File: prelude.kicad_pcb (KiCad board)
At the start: 2 copper layers, 0 parts

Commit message: Several changes
Ran CvPcb
Added MicroSD card connector (Molex)
Started PCB routing with MCU pin row pins 1-16 facing 50-pin LCD connector
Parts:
- added C1: 8p, Capacitors_SMD:C_0805, F.Cu at (194.1, 133.0)
- added C10: 100n, Capacitors_SMD:C_0805, F.Cu at (191.9, 127.6)
- added C11: 22u, Capacitors_SMD:C_0805, F.Cu at (203.4, 119.1)
- added C12: 100n, Capacitors_SMD:C_0805, F.Cu at (208.8, 112.8)
- added C13: 100n, Capacitors_SMD:C_0805, F.Cu at (196.1, 127.5)
- added C14: 1uF, Capacitors_SMD:C_0805, F.Cu at (190.1, 133.3)
- added C15: 1uF, Capacitors_SMD:C_0805, F.Cu at (200.2, 124.4)
- added C2: 8p, Capacitors_SMD:C_0805, F.Cu at (187.8, 127.9)
- added C3: 100n, Capacitors_SMD:C_0805, F.Cu at (207.5, 107.5)
- added C4: 10uF, Capacitors_SMD:C_0805, F.Cu at (200.7, 113.8)
- added C5: 100n, Capacitors_SMD:C_0805, F.Cu at (181.9, 133.4)
- added C6: 1u, Capacitors_SMD:C_0805, F.Cu at (195.2, 122.2)
- added C7: 10u, Capacitors_SMD:C_0805, F.Cu at (204.7, 113.8)
- added C8: 100n, Capacitors_SMD:C_0805, F.Cu at (186.1, 133.4)
- added C9: 100n, Capacitors_SMD:C_0805, F.Cu at (199.3, 119.1)
- added D1: LED, LEDs:LED_0805, F.Cu at (208.9, 118.1)
- added D2: MBR0530, Diodes_SMD:D_SOD-123, F.Cu at (186.0, 122.2)
- added F1: Polyfuse, volium:MF-PSMF050X, F.Cu at (202.0, 108.1)
- added J1: CONN_01X50, volium:62684-502100ALF, F.Cu at (121.7, 137.0)
- added J2: USB_C, volium:DX07S024XJ1, F.Cu at (114.8, 98.3)
- added J3: CONN_01X04, Pin_Headers:Pin_Header_Angled_1x04_Pitch2.54mm, F.Cu at (181.1, 108.3)
- added L1: 2.2uH, Inductors:Inductor_Taiyo-Yuden_NR-24xx, F.Cu at (194.3, 115.9)
- added L2: 22uH, Inductors:Inductor_Taiyo-Yuden_NR-30xx, F.Cu at (173.8, 133.0)
- added R1: 5K1, Resistors_SMD:R_0805, F.Cu at (177.8, 132.2)
- added R2: 5K1, Resistors_SMD:R_0805, F.Cu at (184.1, 128.1)
- added R3: 330, Resistors_SMD:R_0805, F.Cu at (191.4, 122.3)
- added R4: 2.55, Resistors_SMD:R_0805, F.Cu at (168.9, 133.8)
- added R5: 1.5K, Resistors_SMD:R_0805, F.Cu at (109.3, 108.6)
- added SW1: SW_Push, Buttons_Switches_SMD:SW_SPST_PTS645, F.Cu at (177.0, 124.3)
- added U1: LM3671MF-3.3, TO_SOT_Packages_SMD:TSOT-23-5, F.Cu at (153.5, 137.0)
- added U2: STM32F103RETx, Housings_QFP:LQFP-64_10x10mm_Pitch0.5mm, F.Cu at (116.5, 114.9)
- added U3: AP5724, TO_SOT_Packages_SMD:SOT-23-6, F.Cu at (164.0, 135.1)
- added XS1: Molex_microSD_1051620001, volium:Molex_1051620001, F.Cu at (86.4, 112.4)
- added Y1: 16MHz, Crystals:Crystal_SMD_5032-2pin_5.0x3.2mm, F.Cu at (195.3, 108.8)
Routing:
- net /LCD_DB15: track 0.00 -> 39.8 mm, vias 0 -> 2
- net /LCD_DB14: track 0.00 -> 39.4 mm, vias 0 -> 2
- net /LCD_DB13: track 0.00 -> 39.0 mm, vias 0 -> 2
- net /LCD_DB12: track 0.00 -> 38.5 mm, vias 0 -> 2
- net /SDIO_D1: track 0.00 -> 37.2 mm, vias 0 -> 2
- net /SDIO_D0: track 0.00 -> 37.1 mm, vias 0 -> 2
- net /LCD_DB11: track 0.00 -> 35.6 mm, vias 0 -> 2
- net /LCD_RD: track 0.00 -> 35.4 mm
- net /LCD_WR: track 0.00 -> 34.3 mm
- net /LCD_DB3: track 0.00 -> 31.3 mm, vias 0 -> 2
- net /LCD_DB4: track 0.00 -> 30.4 mm, vias 0 -> 2
- net /SDIO_D2: track 0.00 -> 30.1 mm, vias 0 -> 2
- net /LCD_DB5: track 0.00 -> 29.1 mm, vias 0 -> 2
- net /SDIO_D3: track 0.00 -> 28.9 mm, vias 0 -> 2
- net /SDIO_CLK: track 0.00 -> 28.5 mm
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
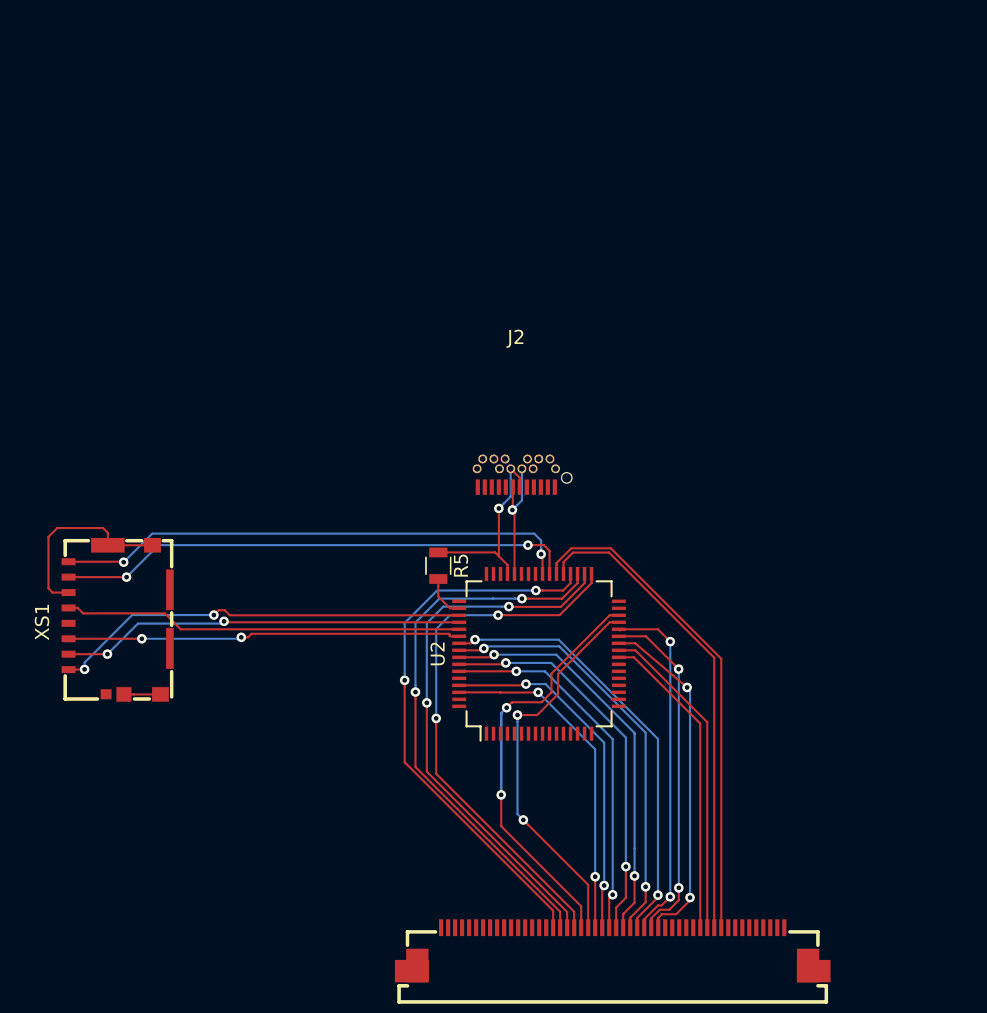
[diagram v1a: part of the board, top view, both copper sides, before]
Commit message: Moved to STM32F411RE
Had to move to different MCU (STM32F411RE) because I2C bus was fixed to pins on B bus, which was used for LCD data bus, and SDIO was also fixed to C bus.
Remapped LCD data bus to C bus since it allows having all other functionality (SDIO, I2C, USB) correctly mapped.
Redid CvPcb and net generation.
Started PCB routing with MCU pins 49-64 facing LCD connector.
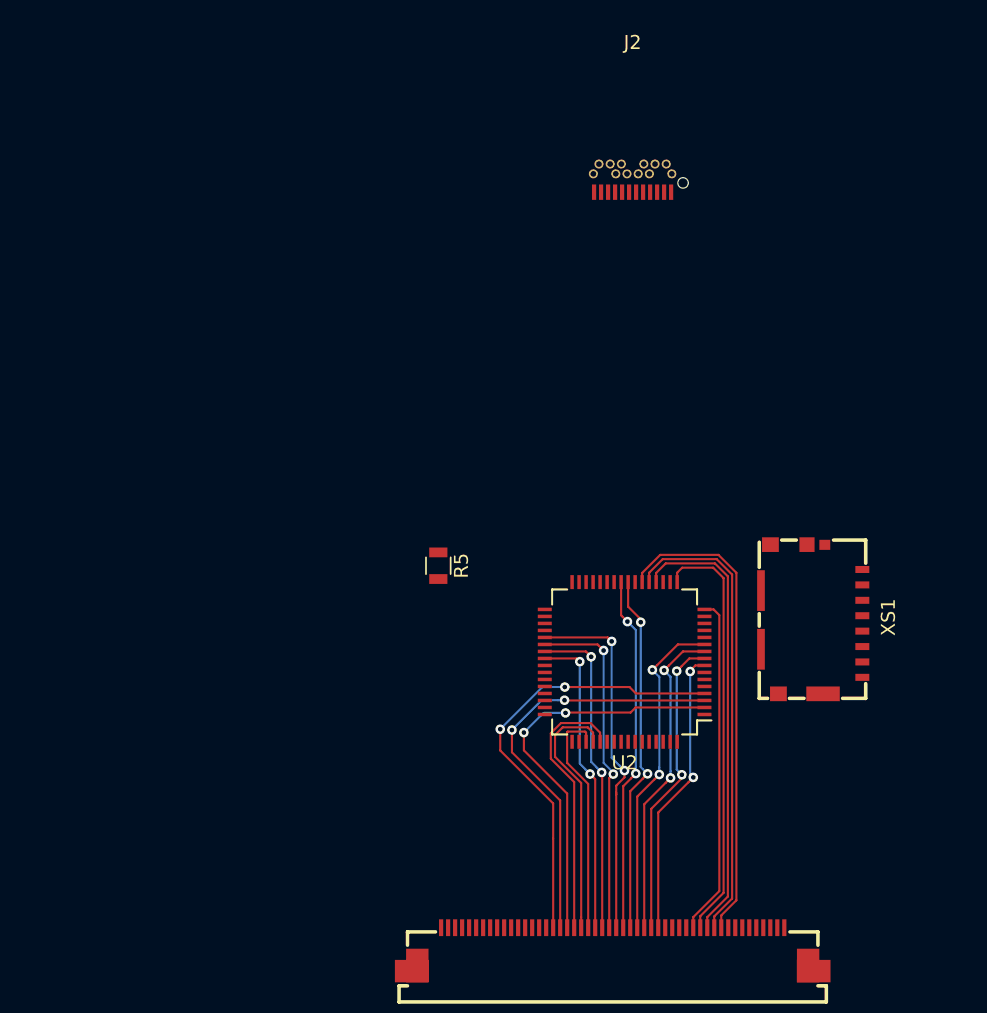
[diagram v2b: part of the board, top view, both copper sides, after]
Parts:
- C13: value 100n -> 4.7u LowESR < 1Ω Ceramic
- R5: value 1.5K -> 10K
- U2: value STM32F103RETx -> STM32F411RETx
- moved XS1 49.5 mm to (136.0, 112.4), turned to 90 degrees
- moved J2 22.6 mm to (123.1, 77.2)
- moved U2 6.14 mm to (122.6, 115.4), turned to 180 degrees
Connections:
- C13 pad 1: +3V3 -> Net-(C13-Pad1)
- J1 pad 1: Net-(J1-Pad1) -> (no net)
- J1 pad 10: Net-(J1-Pad10) -> (no net)
- J1 pad 11: Net-(J1-Pad11) -> (no net)
- J1 pad 12: Net-(J1-Pad12) -> (no net)
- J1 pad 13: Net-(J1-Pad13) -> (no net)
- J1 pad 14: Net-(J1-Pad14) -> (no net)
- J1 pad 15: Net-(J1-Pad15) -> (no net)
- J1 pad 16: Net-(J1-Pad16) -> (no net)
- J1 pad 2: Net-(J1-Pad2) -> (no net)
- J1 pad 3: Net-(J1-Pad3) -> (no net)
- J1 pad 33: Net-(J1-Pad33) -> (no net)
- J1 pad 34: Net-(J1-Pad34) -> (no net)
- J1 pad 35: Net-(J1-Pad35) -> (no net)
- J1 pad 36: /LCD_IMO -> (no net)
- J1 pad 4: Net-(J1-Pad4) -> (no net)
- J1 pad 42: Net-(J1-Pad42) -> (no net)
- J1 pad 43: Net-(J1-Pad43) -> (no net)
- J1 pad 44: Net-(J1-Pad44) -> (no net)
- J1 pad 45: Net-(J1-Pad45) -> (no net)
- J1 pad 46: Net-(J1-Pad46) -> (no net)
- J1 pad 47: Net-(J1-Pad47) -> (no net)
- J1 pad 48: Net-(J1-Pad48) -> (no net)
- J1 pad 9: Net-(J1-Pad9) -> (no net)
- J2 pad A10: Net-(J2-PadA10) -> (no net)
- J2 pad A11: Net-(J2-PadA11) -> (no net)
- J2 pad A2: Net-(J2-PadA2) -> (no net)
- J2 pad A3: Net-(J2-PadA3) -> (no net)
- J2 pad A8: Net-(J2-PadA8) -> (no net)
- J2 pad B10: Net-(J2-PadB10) -> (no net)
- J2 pad B11: Net-(J2-PadB11) -> (no net)
- J2 pad B2: Net-(J2-PadB2) -> (no net)
- J2 pad B3: Net-(J2-PadB3) -> (no net)
- J2 pad B8: Net-(J2-PadB8) -> (no net)
- R5 pad 1: /USB_DP -> Net-(R5-Pad1)
- R5 pad 2: /USB_EN -> GND
- U1 pad 3: /VCC -> (no net)
- U2 pad 10: Net-(U2-Pad10) -> /LCD_DB2
- U2 pad 11: /LCD_RST -> /LCD_DB3
- U2 pad 14: Net-(U2-Pad14) -> (no net)
- U2 pad 15: Net-(U2-Pad15) -> (no net)
- U2 pad 16: Net-(U2-Pad16) -> /LCD_RST
- U2 pad 17: Net-(U2-Pad17) -> /LCD_CS
- U2 pad 2: /SDIO_CD -> /LCD_DB13
- U2 pad 20: Net-(U2-Pad20) -> /LCD_RS
- U2 pad 21: Net-(U2-Pad21) -> /LCD_WR
- U2 pad 22: Net-(U2-Pad22) -> /LCD_RD
- U2 pad 23: Net-(U2-Pad23) -> /SDIO_CD
- U2 pad 24: /LCD_CS -> /LCD_DB4
- U2 pad 25: /LCD_RS -> /LCD_DB5
- U2 pad 26: /LCD_DB0 -> (no net)
- U2 pad 27: /LCD_DB1 -> (no net)
- U2 pad 28: /LCD_DB2 -> (no net)
- U2 pad 29: /LCD_DB10 -> (no net)
- U2 pad 3: Net-(U2-Pad3) -> /LCD_DB14
- U2 pad 30: /LCD_DB11 -> Net-(C13-Pad1)
- U2 pad 33: /LCD_DB12 -> (no net)
- U2 pad 34: /LCD_DB13 -> (no net)
- U2 pad 35: /LCD_DB14 -> (no net)
- U2 pad 36: /LCD_DB15 -> /SDIO_CLK
- U2 pad 37: /LCD_WR -> /LCD_DB6
- U2 pad 38: /LCD_RD -> /LCD_DB7
- U2 pad 39: /SDIO_D0 -> /LCD_DB8
- U2 pad 4: Net-(U2-Pad4) -> /LCD_DB15
- U2 pad 40: /SDIO_D1 -> /LCD_DB9
- U2 pad 41: Net-(U2-Pad41) -> /SDIO_D1
- U2 pad 42: Net-(U2-Pad42) -> /SDIO_D2
- U2 pad 43: Net-(U2-Pad43) -> (no net)
- U2 pad 50: /USB_EN -> (no net)
- U2 pad 51: /SDIO_D2 -> /LCD_DB10
- U2 pad 52: /SDIO_D3 -> /LCD_DB11
- U2 pad 53: /SDIO_CLK -> /LCD_DB12
- U2 pad 55: /LCD_DB3 -> (no net)
- U2 pad 56: /LCD_DB4 -> /SDIO_D0
- U2 pad 57: /LCD_DB5 -> /SDIO_D3
- U2 pad 58: /LCD_DB6 -> (no net)
- U2 pad 59: /LCD_DB7 -> (no net)
- U2 pad 60: GND -> Net-(R5-Pad1)
- U2 pad 61: /LCD_DB8 -> (no net)
- U2 pad 62: /LCD_DB9 -> (no net)
- U2 pad 8: Net-(U2-Pad8) -> /LCD_DB0
- U2 pad 9: Net-(U2-Pad9) -> /LCD_DB1
- U3 pad 2: Net-(U3-Pad2) -> (no net)
- U3 pad 4: /LED_CTRL -> (no net)
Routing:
- net /SDIO_D1: track 37.2 -> 0.00 mm, vias 2 -> 0
- net /SDIO_D0: track 37.1 -> 0.00 mm, vias 2 -> 0
- net /SDIO_D2: track 30.1 -> 0.00 mm, vias 2 -> 0
- net /SDIO_D3: track 28.9 -> 0.00 mm, vias 2 -> 0
- net /SDIO_CLK: track 28.5 -> 0.00 mm
- net /SDIO_CMD: track 28.2 -> 0.00 mm, vias 2 -> 0
- net /LCD_RST: track 0.00 -> 24.3 mm
- net /LCD_DB12: track 38.5 -> 19.3 mm, vias 2 -> 0
- net /LCD_DB11: track 35.6 -> 18.3 mm, vias 2 -> 0
- net GND: track 16.6 -> 0.00 mm
- net /USB_DP: track 14.1 -> 0.00 mm, vias 1 -> 0
- net /LCD_DB10: track 28.1 -> 16.6 mm, vias 2 -> 0
- net /LCD_DB13: track 39.0 -> 28.8 mm
- net /USB_DM: track 9.50 -> 0.00 mm, vias 1 -> 0
- net /LCD_DB14: track 39.4 -> 30.2 mm
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
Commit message: A lot of changes, just need to add more polish and clean up
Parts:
- added J4: CONN_01X08, volium:WE_68710814022, F.Cu at (153.8, 82.6)
- J2: footprint volium:DX07S024XJ1 -> volium:Amphenol_12401548E4#2A
- J3: footprint Pin_Headers:Pin_Header_Angled_1x04_Pitch2.54mm -> volium:M20-8890445
- XS1: value Molex_microSD_1051620001 -> SD_ebay-uSD-push/push_SMD; footprint volium:Molex_1051620001 -> volium:Conn_uSDcard
- moved R4 89.0 mm to (163.0, 45.0)
- moved U3 87.1 mm to (163.0, 48.0), turned to 180 degrees
- moved C15 86.6 mm to (159.5, 48.0), turned to 270 degrees
- moved U1 83.3 mm to (175.0, 56.5), turned to 270 degrees
- moved R1 82.8 mm to (167.5, 50.0)
- moved C14 81.1 mm to (163.0, 56.8)
- moved L2 79.8 mm to (163.0, 54.0)
- moved R2 76.8 mm to (167.5, 53.1)
- moved C8 75.2 mm to (169.6, 60.0)
- moved D2 75.0 mm to (162.4, 51.0)
- moved C13 73.2 mm to (163.0, 62.2), turned to 180 degrees
- moved C11 72.0 mm to (172.3, 54.2), turned to 90 degrees
- moved D1 71.9 mm to (171.2, 56.8)
- moved R5 71.3 mm to (174.0, 78.5), turned to 180 degrees
- moved R3 71.3 mm to (170.2, 54.2), turned to 90 degrees
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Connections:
- C4 pad 1: Net-(C4-Pad1) -> /VCC
- F1 pad 1: Net-(C4-Pad1) -> /VCC
- J2 pad A6: /USB_DP -> /USB_D+
- J2 pad A7: /USB_DM -> /USB_D-
- J2 pad B6: /USB_DP -> (no net)
- J2 pad B7: /USB_DM -> (no net)
- U1 pad 1: Net-(C4-Pad1) -> /VCC
- U1 pad 3: (no net) -> /VCC
- U2 pad 14: (no net) -> /LED_CTRL
- U2 pad 16: /LCD_RST -> (no net)
- U2 pad 17: /LCD_CS -> /LCD_RD
- U2 pad 20: /LCD_RS -> /LCD_WR
- U2 pad 21: /LCD_WR -> /LCD_RS
- U2 pad 22: /LCD_RD -> /LCD_CS
- U2 pad 23: /SDIO_CD -> /LCD_RST
- U2 pad 44: /USB_DM -> /USB_D-
- U2 pad 45: /USB_DP -> /USB_D+
- U2 pad 50: (no net) -> /SDIO_CD
- U2 pad 58: (no net) -> /TS_SCL
- U2 pad 59: (no net) -> /TS_SDA
- U2 pad 61: (no net) -> /TS_INT
- U2 pad 62: (no net) -> /TS_RST
- U3 pad 2: (no net) -> GND
- U3 pad 4: (no net) -> /LED_CTRL
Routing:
- net GND: track 0.00 -> 207.6 mm, vias 0 -> 12
- net +3V3: track 0.00 -> 204.7 mm, vias 0 -> 4
- net /LED_K: track 0.00 -> 61.5 mm
- net /LED_A: track 0.00 -> 56.6 mm
- net /NRST: track 0.00 -> 47.0 mm, vias 0 -> 2
- net /SWDIO: track 0.00 -> 43.8 mm, vias 0 -> 2
- net /SWCLK: track 0.00 -> 43.3 mm, vias 0 -> 2
- net /SDIO_CLK: track 0.00 -> 43.0 mm, vias 0 -> 2
- net /USB_D+: track 0.00 -> 37.3 mm, vias 0 -> 2
- net /USB_D-: track 0.00 -> 36.6 mm, vias 0 -> 2
- net /SDIO_D2: track 0.00 -> 35.4 mm, vias 0 -> 2
- net /SDIO_D1: track 0.00 -> 28.9 mm, vias 0 -> 2
- net Net-(J2-PadA5): track 0.00 -> 28.3 mm, vias 0 -> 2
- net /LED_CTRL: track 0.00 -> 27.7 mm, vias 0 -> 2
- net /SDIO_CMD: track 0.00 -> 20.2 mm, vias 0 -> 2
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- added copper zone on B.Cu, net GND
- added copper zone on F.Cu, net GND
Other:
- board outline added: 80 x 60 mm
